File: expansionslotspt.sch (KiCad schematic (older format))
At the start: 2 parts

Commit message: Added D3xx selection logic for PIA (6520) if needed
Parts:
- added R11, R12: 0, Resistors_SMD:R_1206_HandSoldering, symbol R
- added U15, U16: 74LS08, Housings_SSOP:SSOP-14_5.3x6.2mm_Pitch0.65mm, symbol 74LS08
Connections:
- net labels added: VCC3V3, mA15, mD3XX, ~mA10, ~mA11, ~mA13
- wire segments 0 -> 15
- no-connect marks 0 -> 1
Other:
- note added: "D3xx address select (PIA 6520)"
- moved on the sheet: CART2, ECI2

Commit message: Modified for new MCU
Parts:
- removed R11, R12: 0, Resistors_SMD:R_1206_HandSoldering, symbol R
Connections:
- net labels added: DXXX, mA10, mA12, mA14, mA8, mA9, mD6XX, ~mA11mA9, ~mA8
- wire segments 15 -> 10
- no-connect marks 1 -> 0
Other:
- note added: "D6xx address select"
- note added: "DXXX address select"
- moved on the sheet: U15C, U15D, U16A, U16B, U16C, U16D

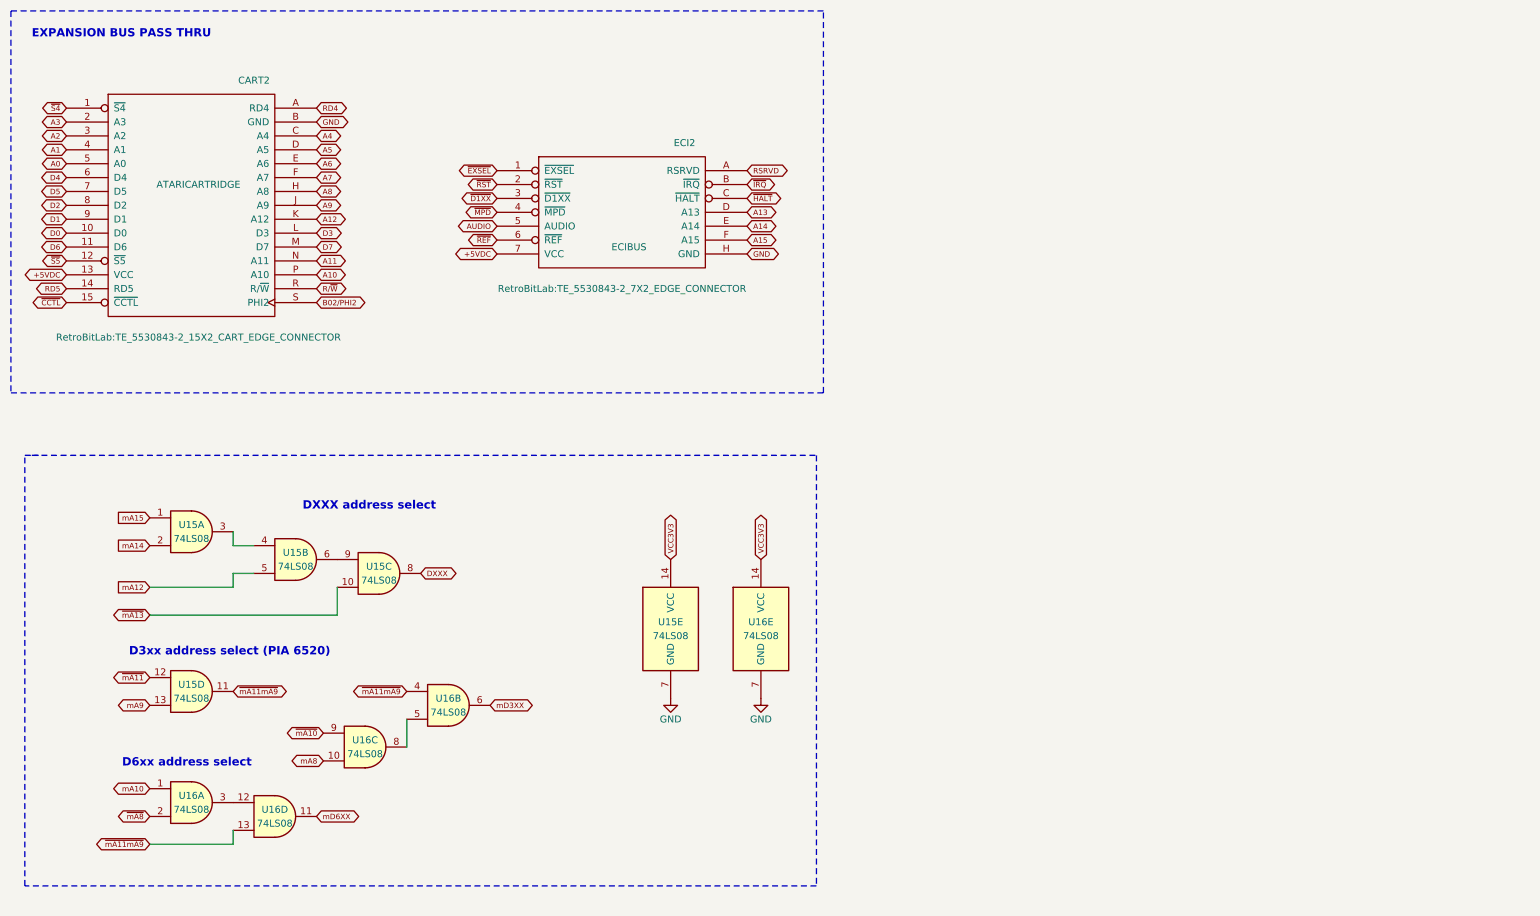
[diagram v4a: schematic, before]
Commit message: Corrected MCU and Global Net List Name for Address Selection D6xx and D3xx
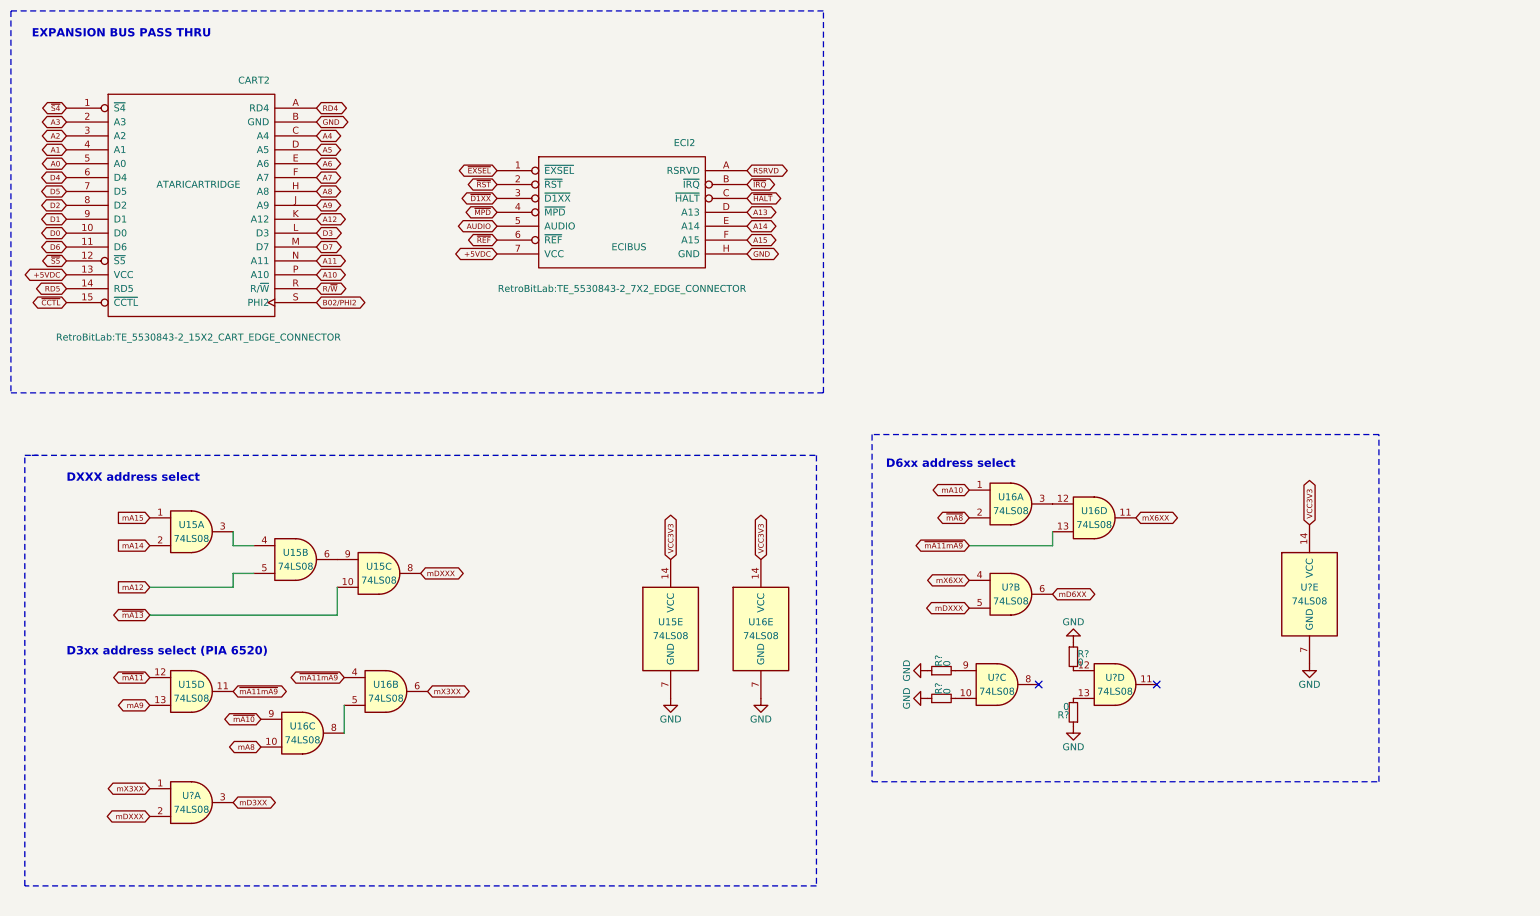
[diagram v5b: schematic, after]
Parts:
- added R? (x4): 0, symbol R_Small
- added U? (x5): 74LS08, symbol 74LS08
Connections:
- net GND: now also R?.1, R?.1, R?.1, R?.1, U?.7 (GND)
- net VCC3V3: now also U?.14 (VCC)
- net mD3XX: now also U?.3; no longer U16.6
- net mD6XX: now also U?.6; no longer U16.11
- net DXXX renamed mDXXX
- net mDXXX: now also U?.2, U?.5
- new net: R?.2, U?.10
- new net: R?.2, U?.9
- new net: R?.2, U?.12
- new net: R?.2, U?.13
- new net mX3XX: U16.6, U?.1
- new net mX6XX: U16.11, U?.4
- no-connect marks 0 -> 2
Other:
- moved on the sheet: U16A, U16B, U16C, U16D

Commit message: Transformation will begin shortly... ;-)
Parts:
- R6, R7, R8, R9: renamed from R?; footprint (none) -> Resistors_SMD:R_1206_HandSoldering
- U18: renamed from U?; footprint (none) -> Housings_SSOP:TSSOP-14_4.4x5mm_Pitch0.65mm
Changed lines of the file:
@@
 EESchema Schematic File Version 2
-LIBS:atari23MTS_Upgrade-rescue
-LIBS:power
-LIBS:device
-LIBS:transistors
-LIBS:conn
-LIBS:linear
-LIBS:regul
-LIBS:74xx
-LIBS:cmos4000
-LIBS:adc-dac
-LIBS:memory
-LIBS:xilinx
-LIBS:microcontrollers
-LIBS:dsp
-LIBS:microchip
-LIBS:analog_switches
-LIBS:motorola
-LIBS:texas
-LIBS:intel
-LIBS:audio
-LIBS:interface
-LIBS:digital-audio
-LIBS:philips
-LIBS:display
-LIBS:cypress
-LIBS:siliconi
-LIBS:opto
-LIBS:atmel
-LIBS:contrib
-LIBS:valves
 LIBS:AmigaComponents
 LIBS:4xxx
 LIBS:4xxx_IEEE
 LIBS:74xGxx
+LIBS:74xx
 LIBS:74xx_IEEE
 LIBS:Amplifier_Audio
@@
 LIBS:FPGA_Xilinx_Virtex6
 LIBS:FPGA_Xilinx_Virtex7
+LIBS:ft232rl
 LIBS:GPU
 LIBS:Graphic
@@
 LIBS:Oscillator
 LIBS:Potentiometer_Digital
+LIBS:power
 LIBS:Power_Management
 LIBS:Power_Protection
@@
 $EndComp
 $Comp
-L GND #PWR36
+L GND #PWR037
 U 1 1 5C3CCE15
 P 5950 5800
-F 0 "#PWR36" H 5950 5550 50  0001 C CNN
+F 0 "#PWR037" H 5950 5550 50  0001 C CNN
 F 1 "GND" H 5950 5650 50  0000 C CNN
 F 2 "" H 5950 5800 50  0001 C CNN
@@
 $EndComp
 $Comp
-L GND #PWR35
+L GND #PWR038
 U 1 1 5C3CD0DD
 P 5300 5800
-F 0 "#PWR35" H 5300 5550 50  0001 C CNN
+F 0 "#PWR038" H 5300 5550 50  0001 C CNN
 F 1 "GND" H 5300 5650 50  0000 C CNN
 F 2 "" H 5300 5800 50  0001 C CNN
@@
 mX6XX
 $Comp
-L 74LS08 U?
+L 74LS08 U18
 U 1 1 5C42E852
 P 1850 6550
-F 0 "U?" H 1850 6600 50  0000 C CNN
+F 0 "U18" H 1850 6600 50  0000 C CNN
 F 1 "74LS08" H 1850 6500 50  0000 C CNN
-F 2 "" H 1850 6550 50  0001 C CNN
+F 2 "Housings_SSOP:TSSOP-14_4.4x5mm_Pitch0.65mm" H 1850 6550 50  0001 C CNN
 F 3 "" H 1850 6550 50  0001 C CNN
 	1    1850 6550
@@
 mD3XX
 $Comp
-L 74LS08 U?
+L 74LS08 U18
 U 2 1 5C42EC5B
 P 7750 5050
-F 0 "U?" H 7750 5100 50  0000 C CNN
+F 0 "U18" H 7750 5100 50  0000 C CNN
 F 1 "74LS08" H 7750 5000 50  0000 C CNN
-F 2 "" H 7750 5050 50  0001 C CNN
+F 2 "Housings_SSOP:TSSOP-14_4.4x5mm_Pitch0.65mm" H 7750 5050 50  0001 C CNN
 F 3 "" H 7750 5050 50  0001 C CNN
 	2    7750 5050
@@
 mD6XX
 $Comp
-L 74LS08 U?
+L 74LS08 U18
 U 3 1 5C42EDA7
 P 7650 5700
-F 0 "U?" H 7650 5750 50  0000 C CNN
+F 0 "U18" H 7650 5750 50  0000 C CNN
 F 1 "74LS08" H 7650 5650 50  0000 C CNN
-F 2 "" H 7650 5700 50  0001 C CNN
+F 2 "Housings_SSOP:TSSOP-14_4.4x5mm_Pitch0.65mm" H 7650 5700 50  0001 C CNN
 F 3 "" H 7650 5700 50  0001 C CNN
 	3    7650 5700
@@
 $EndComp
 $Comp
-L 74LS08 U?
+L 74LS08 U18
 U 4 1 5C42EE0A
 P 8500 5700
-F 0 "U?" H 8500 5750 50  0000 C CNN
+F 0 "U18" H 8500 5750 50  0000 C CNN
 F 1 "74LS08" H 8500 5650 50  0000 C CNN
-F 2 "" H 8500 5700 50  0001 C CNN
+F 2 "Housings_SSOP:TSSOP-14_4.4x5mm_Pitch0.65mm" H 8500 5700 50  0001 C CNN
 F 3 "" H 8500 5700 50  0001 C CNN
 	4    8500 5700
@@
 $EndComp
 $Comp
-L 74LS08 U?
+L 74LS08 U18
 U 5 1 5C42EE59
 P 9900 5050
-F 0 "U?" H 9900 5100 50  0000 C CNN
+F 0 "U18" H 9900 5100 50  0000 C CNN
 F 1 "74LS08" H 9900 5000 50  0000 C CNN
-F 2 "" H 9900 5050 50  0001 C CNN
+F 2 "Housings_SSOP:TSSOP-14_4.4x5mm_Pitch0.65mm" H 9900 5050 50  0001 C CNN
 F 3 "" H 9900 5050 50  0001 C CNN
 	5    9900 5050
@@
 VCC3V3
 $Comp
-L GND #PWR?
+L GND #PWR039
 U 1 1 5C42EEF4
 P 9900 5550
-F 0 "#PWR?" H 9900 5300 50  0001 C CNN
+F 0 "#PWR039" H 9900 5300 50  0001 C CNN
 F 1 "GND" H 9900 5400 50  0000 C CNN
 F 2 "" H 9900 5550 50  0001 C CNN
@@
 NoConn ~ 7950 5700
 $Comp
-L R_Small R?
+L R_Small R8
 U 1 1 5C42EF4D
 P 8200 5500
-F 0 "R?" H 8230 5520 50  0000 L CNN
+F 0 "R8" H 8230 5520 50  0000 L CNN
 F 1 "0" H 8230 5460 50  0000 L CNN
-F 2 "" H 8200 5500 50  0000 C CNN
+F 2 "Resistors_SMD:R_1206_HandSoldering" H 8200 5500 50  0001 C CNN
 F 3 "" H 8200 5500 50  0000 C CNN
 	1    8200 5500
@@
 $EndComp
 $Comp
-L GND #PWR?
+L GND #PWR040
 U 1 1 5C42F02F
 P 8200 5400
-F 0 "#PWR?" H 8200 5150 50  0001 C CNN
+F 0 "#PWR040" H 8200 5150 50  0001 C CNN
 F 1 "GND" H 8200 5250 50  0000 C CNN
 F 2 "" H 8200 5400 50  0001 C CNN
@@
 $EndComp
 $Comp
-L R_Small R?
+L R_Small R6
 U 1 1 5C42F0BD
 P 7250 5600
-F 0 "R?" H 7280 5620 50  0000 L CNN
+F 0 "R6" H 7280 5620 50  0000 L CNN
 F 1 "0" H 7280 5560 50  0000 L CNN
-F 2 "" H 7250 5600 50  0000 C CNN
+F 2 "Resistors_SMD:R_1206_HandSoldering" H 7250 5600 50  0001 C CNN
 F 3 "" H 7250 5600 50  0000 C CNN
 	1    7250 5600
@@
 $EndComp
 $Comp
-L GND #PWR?
+L GND #PWR041
 U 1 1 5C42F0C3
 P 7150 5600
-F 0 "#PWR?" H 7150 5350 50  0001 C CNN
+F 0 "#PWR041" H 7150 5350 50  0001 C CNN
 F 1 "GND" H 7150 5450 50  0000 C CNN
 F 2 "" H 7150 5600 50  0001 C CNN
@@
 $EndComp
 $Comp
-L R_Small R?
+L R_Small R7
 U 1 1 5C42F15E
 P 7250 5800
-F 0 "R?" H 7280 5820 50  0000 L CNN
+F 0 "R7" H 7280 5820 50  0000 L CNN
 F 1 "0" H 7280 5760 50  0000 L CNN
-F 2 "" H 7250 5800 50  0000 C CNN
+F 2 "Resistors_SMD:R_1206_HandSoldering" H 7250 5800 50  0001 C CNN
 F 3 "" H 7250 5800 50  0000 C CNN
 	1    7250 5800
@@
 $EndComp
 $Comp
-L GND #PWR?
+L GND #PWR042
 U 1 1 5C42F164
 P 7150 5800
-F 0 "#PWR?" H 7150 5550 50  0001 C CNN
+F 0 "#PWR042" H 7150 5550 50  0001 C CNN
 F 1 "GND" H 7150 5650 50  0000 C CNN
 F 2 "" H 7150 5800 50  0001 C CNN
@@
 $EndComp
 $Comp
-L R_Small R?
+L R_Small R9
 U 1 1 5C42F223
 P 8200 5900
-F 0 "R?" H 8230 5920 50  0000 L CNN
+F 0 "R9" H 8230 5920 50  0000 L CNN
 F 1 "0" H 8230 5860 50  0000 L CNN
-F 2 "" H 8200 5900 50  0000 C CNN
+F 2 "Resistors_SMD:R_1206_HandSoldering" H 8200 5900 50  0001 C CNN
 F 3 "" H 8200 5900 50  0000 C CNN
 	1    8200 5900
@@
 $EndComp
 $Comp
-L GND #PWR?
+L GND #PWR043
 U 1 1 5C42F229
 P 8200 6000
-F 0 "#PWR?" H 8200 5750 50  0001 C CNN
+F 0 "#PWR043" H 8200 5750 50  0001 C CNN
 F 1 "GND" H 8200 5850 50  0000 C CNN
 F 2 "" H 8200 6000 50  0001 C CNN

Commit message: Multiple library support for Kicad. Need a reconfiguration at work
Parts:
- renumbered R6 to R4, R7 to R5, R8 to R6, R9 to R7, U15 to U14, U16 to U14, U16 to U15, U18 to U15, U18 to U16
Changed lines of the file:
@@
 EXPANSION BUS PASS THRU
 $Comp
-L 74LS08 U15
+L 74LS08 U14
 U 1 1 5C3CC31E
 P 1850 4600
-F 0 "U15" H 1850 4650 50  0000 C CNN
+F 0 "U14" H 1850 4650 50  0000 C CNN
 F 1 "74LS08" H 1850 4550 50  0000 C CNN
 F 2 "Housings_SSOP:SSOP-14_5.3x6.2mm_Pitch0.65mm" H 1850 4600 50  0001 C CNN
@@
 $EndComp
 $Comp
-L 74LS08 U15
+L 74LS08 U14
 U 2 1 5C3CC3C3
 P 2600 4800
-F 0 "U15" H 2600 4850 50  0000 C CNN
+F 0 "U14" H 2600 4850 50  0000 C CNN
 F 1 "74LS08" H 2600 4750 50  0000 C CNN
 F 2 "Housings_SSOP:SSOP-14_5.3x6.2mm_Pitch0.65mm" H 2600 4800 50  0001 C CNN
@@
 $EndComp
 $Comp
-L 74LS08 U16
+L 74LS08 U15
 U 4 1 5C3CC52F
 P 8350 4500
-F 0 "U16" H 8350 4550 50  0000 C CNN
+F 0 "U15" H 8350 4550 50  0000 C CNN
 F 1 "74LS08" H 8350 4450 50  0000 C CNN
 F 2 "Housings_SSOP:SSOP-14_5.3x6.2mm_Pitch0.65mm" H 8350 4500 50  0001 C CNN
@@
 $EndComp
 $Comp
-L 74LS08 U15
+L 74LS08 U14
 U 5 1 5C3CC5C2
 P 5300 5300
-F 0 "U15" H 5300 5350 50  0000 C CNN
+F 0 "U14" H 5300 5350 50  0000 C CNN
 F 1 "74LS08" H 5300 5250 50  0000 C CNN
 F 2 "Housings_SSOP:SSOP-14_5.3x6.2mm_Pitch0.65mm" H 5300 5300 50  0001 C CNN
@@
 $EndComp
 $Comp
-L 74LS08 U16
+L 74LS08 U15
 U 2 1 5C3CC6CE
 P 3250 5750
-F 0 "U16" H 3250 5800 50  0000 C CNN
+F 0 "U15" H 3250 5800 50  0000 C CNN
 F 1 "74LS08" H 3250 5700 50  0000 C CNN
 F 2 "Housings_SSOP:SSOP-14_5.3x6.2mm_Pitch0.65mm" H 3250 5750 50  0001 C CNN
@@
 $EndComp
 $Comp
-L 74LS08 U16
+L 74LS08 U14
 U 3 1 5C3CC75B
 P 2650 6050
-F 0 "U16" H 2650 6100 50  0000 C CNN
+F 0 "U14" H 2650 6100 50  0000 C CNN
 F 1 "74LS08" H 2650 6000 50  0000 C CNN
 F 2 "Housings_SSOP:SSOP-14_5.3x6.2mm_Pitch0.65mm" H 2650 6050 50  0001 C CNN
@@
 mX3XX
 $Comp
-L 74LS08 U15
+L 74LS08 U14
 U 4 1 5C3CCCA1
 P 1850 5750
-F 0 "U15" H 1850 5800 50  0000 C CNN
+F 0 "U14" H 1850 5800 50  0000 C CNN
 F 1 "74LS08" H 1850 5700 50  0000 C CNN
 F 2 "Housings_SSOP:SSOP-14_5.3x6.2mm_Pitch0.65mm" H 1850 5750 50  0001 C CNN
@@
 $EndComp
 $Comp
-L 74LS08 U16
+L 74LS08 U15
 U 5 1 5C3CCD66
 P 5950 5300
-F 0 "U16" H 5950 5350 50  0000 C CNN
+F 0 "U15" H 5950 5350 50  0000 C CNN
 F 1 "74LS08" H 5950 5250 50  0000 C CNN
 F 2 "Housings_SSOP:SSOP-14_5.3x6.2mm_Pitch0.65mm" H 5950 5300 50  0001 C CNN
@@
 mX6XX
 $Comp
-L 74LS08 U18
+L 74LS08 U15
 U 1 1 5C42E852
 P 1850 6550
-F 0 "U18" H 1850 6600 50  0000 C CNN
+F 0 "U15" H 1850 6600 50  0000 C CNN
 F 1 "74LS08" H 1850 6500 50  0000 C CNN
 F 2 "Housings_SSOP:TSSOP-14_4.4x5mm_Pitch0.65mm" H 1850 6550 50  0001 C CNN
@@
 mD3XX
 $Comp
-L 74LS08 U18
+L 74LS08 U16
 U 2 1 5C42EC5B
 P 7750 5050
-F 0 "U18" H 7750 5100 50  0000 C CNN
+F 0 "U16" H 7750 5100 50  0000 C CNN
 F 1 "74LS08" H 7750 5000 50  0000 C CNN
 F 2 "Housings_SSOP:TSSOP-14_4.4x5mm_Pitch0.65mm" H 7750 5050 50  0001 C CNN
@@
 mD6XX
 $Comp
-L 74LS08 U18
+L 74LS08 U16
 U 3 1 5C42EDA7
 P 7650 5700
-F 0 "U18" H 7650 5750 50  0000 C CNN
+F 0 "U16" H 7650 5750 50  0000 C CNN
 F 1 "74LS08" H 7650 5650 50  0000 C CNN
 F 2 "Housings_SSOP:TSSOP-14_4.4x5mm_Pitch0.65mm" H 7650 5700 50  0001 C CNN
@@
 $EndComp
 $Comp
-L 74LS08 U18
+L 74LS08 U16
 U 4 1 5C42EE0A
 P 8500 5700
-F 0 "U18" H 8500 5750 50  0000 C CNN
+F 0 "U16" H 8500 5750 50  0000 C CNN
 F 1 "74LS08" H 8500 5650 50  0000 C CNN
 F 2 "Housings_SSOP:TSSOP-14_4.4x5mm_Pitch0.65mm" H 8500 5700 50  0001 C CNN
@@
 $EndComp
 $Comp
-L 74LS08 U18
+L 74LS08 U16
 U 5 1 5C42EE59
 P 9900 5050
-F 0 "U18" H 9900 5100 50  0000 C CNN
+F 0 "U16" H 9900 5100 50  0000 C CNN
 F 1 "74LS08" H 9900 5000 50  0000 C CNN
 F 2 "Housings_SSOP:TSSOP-14_4.4x5mm_Pitch0.65mm" H 9900 5050 50  0001 C CNN
@@
 NoConn ~ 7950 5700
 $Comp
-L R_Small R8
+L R_Small R6
 U 1 1 5C42EF4D
 P 8200 5500
-F 0 "R8" H 8230 5520 50  0000 L CNN
+F 0 "R6" H 8230 5520 50  0000 L CNN
 F 1 "0" H 8230 5460 50  0000 L CNN
 F 2 "Resistors_SMD:R_1206_HandSoldering" H 8200 5500 50  0001 C CNN
@@
 $EndComp
 $Comp
-L R_Small R6
+L R_Small R4
 U 1 1 5C42F0BD
 P 7250 5600
-F 0 "R6" H 7280 5620 50  0000 L CNN
+F 0 "R4" H 7280 5620 50  0000 L CNN
 F 1 "0" H 7280 5560 50  0000 L CNN
 F 2 "Resistors_SMD:R_1206_HandSoldering" H 7250 5600 50  0001 C CNN
@@
 $EndComp
 $Comp
-L R_Small R7
+L R_Small R5
 U 1 1 5C42F15E
 P 7250 5800
-F 0 "R7" H 7280 5820 50  0000 L CNN
+F 0 "R5" H 7280 5820 50  0000 L CNN
 F 1 "0" H 7280 5760 50  0000 L CNN
 F 2 "Resistors_SMD:R_1206_HandSoldering" H 7250 5800 50  0001 C CNN
@@
 $EndComp
 $Comp
-L R_Small R9
+L R_Small R7
 U 1 1 5C42F223
 P 8200 5900
-F 0 "R9" H 8230 5920 50  0000 L CNN
+F 0 "R7" H 8230 5920 50  0000 L CNN
 F 1 "0" H 8230 5860 50  0000 L CNN
 F 2 "Resistors_SMD:R_1206_HandSoldering" H 8200 5900 50  0001 C CNN
